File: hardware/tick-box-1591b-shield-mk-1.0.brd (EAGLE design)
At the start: 90 x 57 mm, 15 parts, among them IC1 DS3231, U1 ARDUINO_SHIELDINSIDER

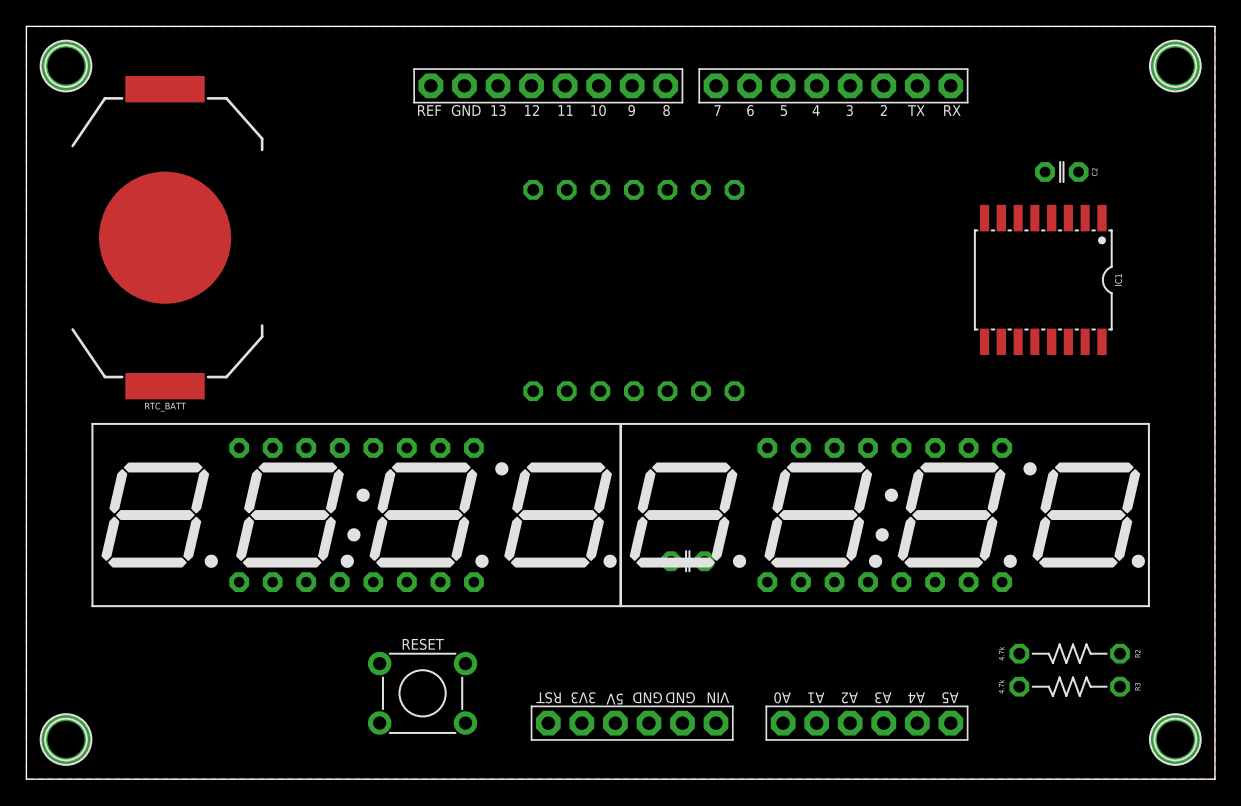
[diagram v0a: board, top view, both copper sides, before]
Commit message: clocks are hard, some more stabs
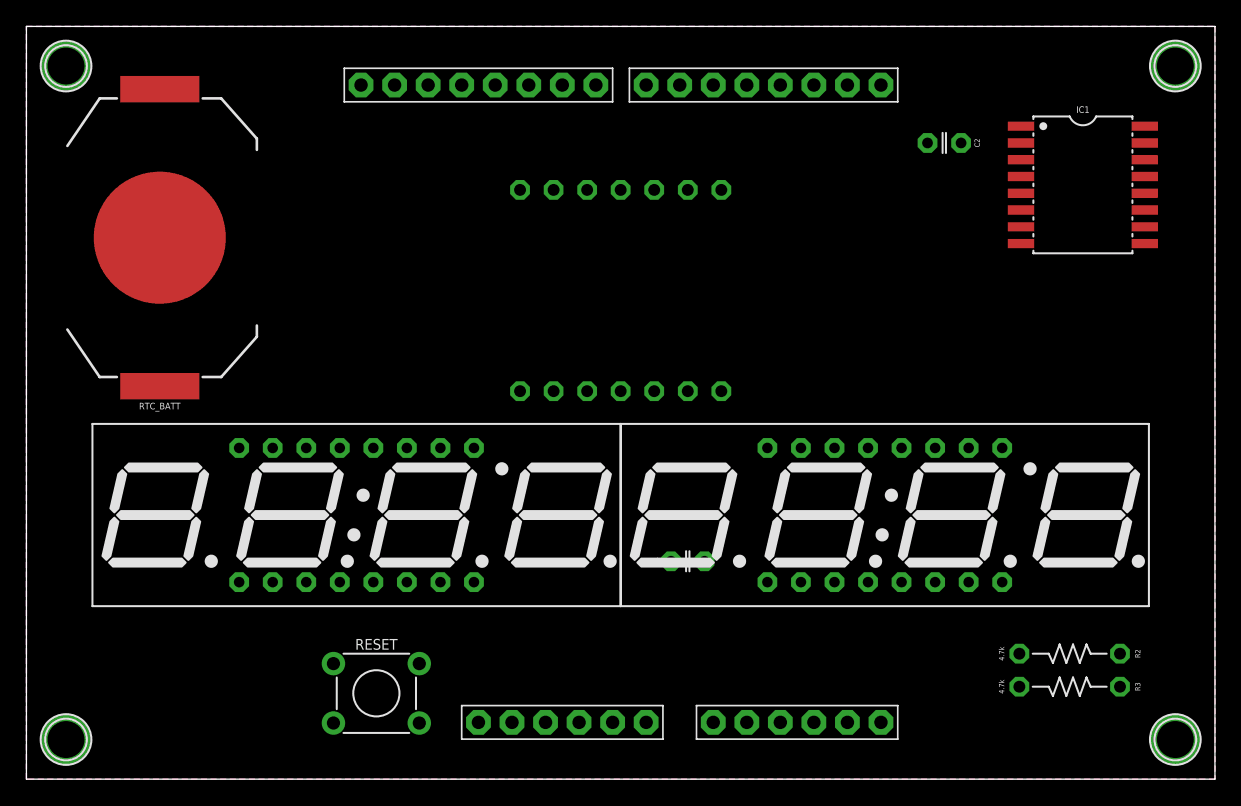
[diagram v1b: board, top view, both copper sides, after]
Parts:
- U1: value ARDUINO_SHIELDINSIDER -> ARDUINO_SHIELDNOOUTLINE_NOHOLES; device A_butts:ARDUINO_SHIELD_NOOUTLINE_INSIDE -> A_butts:ARDUINO_SHIELD_NOOUTLINE_NOHOLES
- moved U1 46.1 mm to (24.0, 55.0)
- moved C2 9.17 mm to (69.5, 48.2)
- moved IC1 7.80 mm to (80.0, 45.0), turned to 270 degrees
- moved RESET 3.50 mm to (26.5, 6.50)
- moved DISPLAY1 1.00 mm to (45.0, 37.0)
- moved RTC_BATT 0.40 mm to (10.1, 41.0)
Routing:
- added copper zone on layer 16, net GND
